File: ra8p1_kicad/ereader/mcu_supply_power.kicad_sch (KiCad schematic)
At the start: 20 parts, among them U1 R7KA8P1KFLCAC#UC0

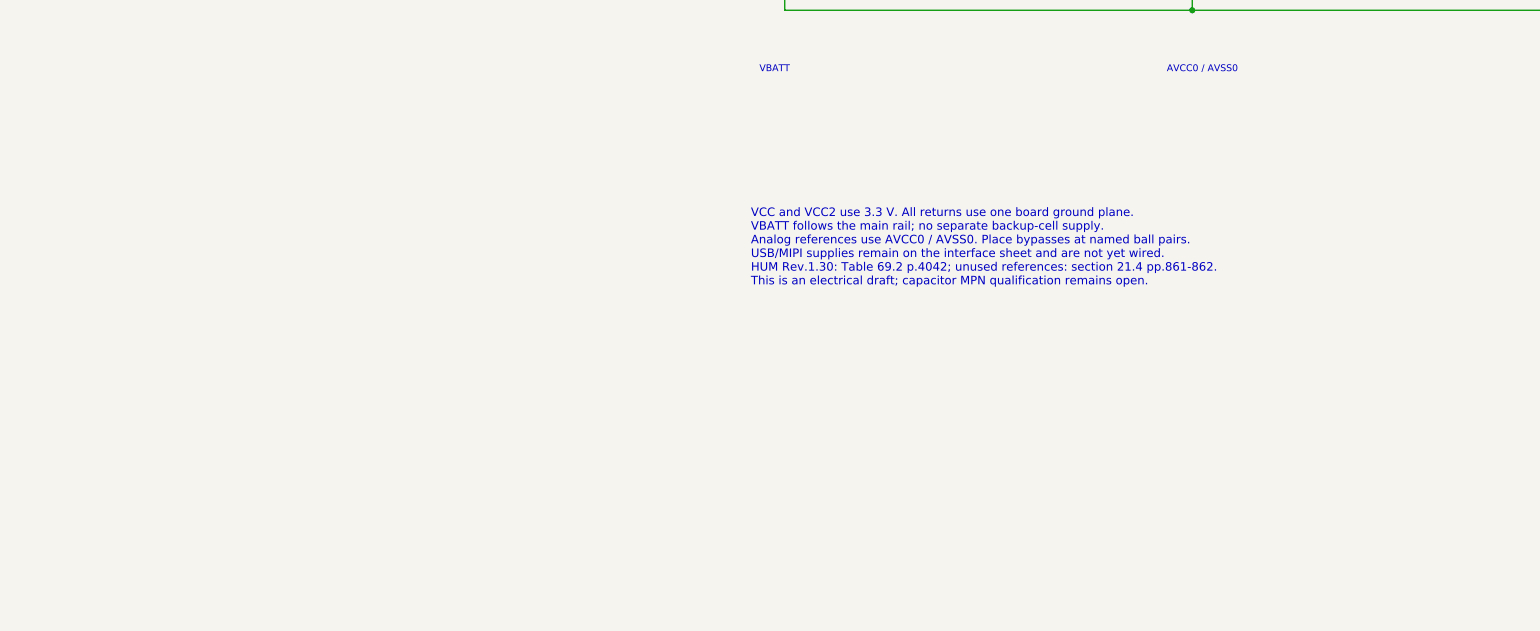
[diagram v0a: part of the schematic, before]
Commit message: hardware: integrate MIPI host 1.8V supply and bypass (#824, #841)
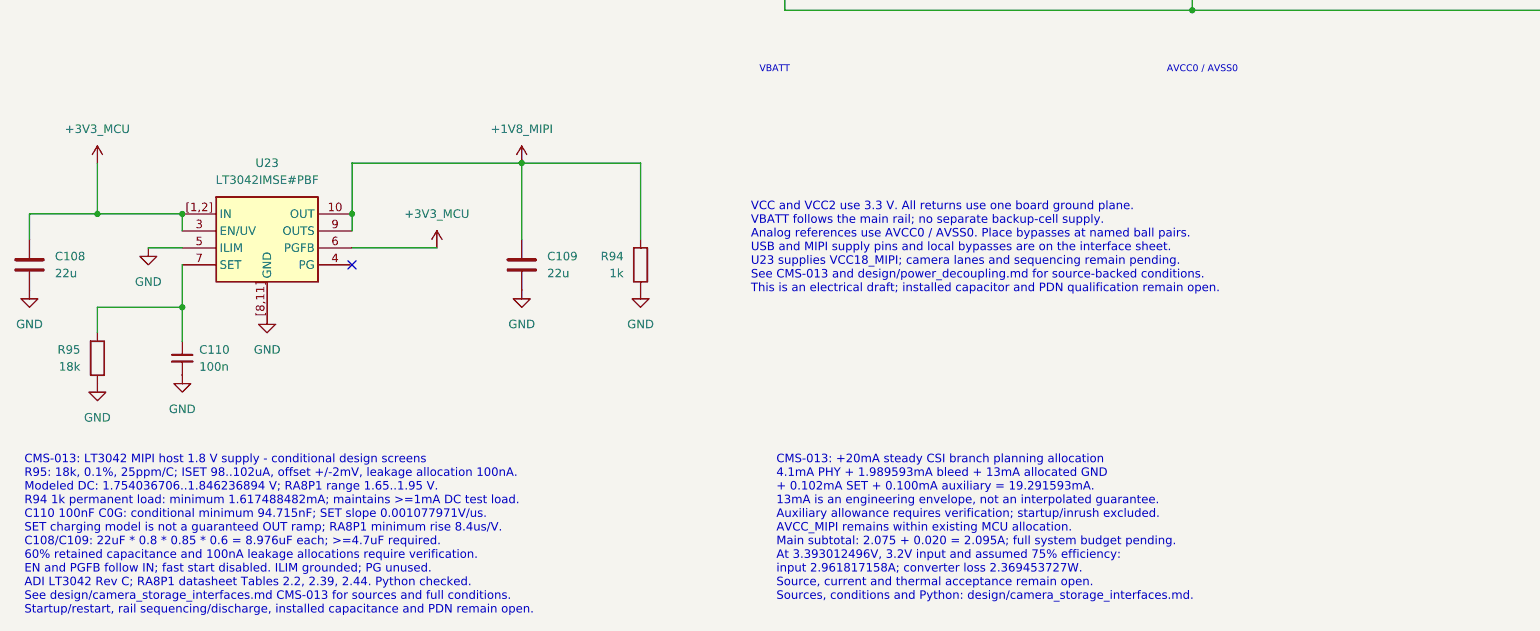
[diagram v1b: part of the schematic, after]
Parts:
- added C108, C109: 22u, symbol Device:C
- added C110: 100n, symbol Device:C_Small
- added R94: 1k, symbol Device:R
- added R95: 18k, symbol Device:R
- added U23: LT3042IMSE#PBF, Package_SO:MSOP-10-1EP_3x3mm_P0.5mm_EP1.68x1.88mm, symbol Power_Devices:LT3042IMSE#PBF
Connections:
- net +3V3_MCU: now also C108.1, U23.3 (EN/UV), U23.6 (PGFB), U23.[1,2] (IN)
- net GND: now also C108.2, C109.2, C110.2, R94.1, R95.1, U23.5 (ILIM), U23.[8,11] (GND)
- new net: C110.1, R95.2, U23.7 (SET)
- new net +1V8_MIPI: C109.1, R94.2, U23.10 (OUT), U23.9 (OUTS)
- no-connect marks 0 -> 1
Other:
- note added: "CMS-013: +20mA steady CSI branch planning allocation 4.1mA PHY + 1.989593mA bleed + 13mA allocated GND + 0.102mA SET + 0.100mA auxiliary = 19.291593mA. 13mA is an engineering envelope, not an interpolated guarantee. Auxiliary allowance requires verification; startup/inrush excluded. AVCC_MIPI remains within existing MCU allocation. Main subtotal: 2.075 + 0.020 = 2.095A; full system budget pending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"
- note added: "CMS-013: LT3042 MIPI host 1.8 V supply - conditional design screens R95: 18k, 0.1%, 25ppm/C; ISET 98..102uA, offset +/-2mV, leakage allocation 100nA. Modeled DC: 1.754036706..1.846236894 V; RA8P1 range 1.65..1.95 V. R94 1k permanent load: minimum 1.617488482mA; maintains >=1mA DC test load. C110 100nF C0G: conditional minimum 94.715nF; SET slope 0.001077971V/us. SET charging model is not a guaran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"
- note added: "VCC and VCC2 use 3.3 V. All returns use one board ground plane. VBATT follows the main rail; no separate backup-cell supply. Analog references use AVCC0 / AVSS0. Place bypasses at named ball pairs. USB and MIPI supply pins and local bypasses are on the interface sheet. U23 supplies VCC18_MIPI; camera lanes and sequencing remain pending. See CMS-013 and design/power_decoupling.md for source-backed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"
- note removed: "VCC and VCC2 use 3.3 V. All returns use one board ground plane. VBATT follows the main rail; no separate backup-cell supply. Analog references use AVCC0 / AVSS0. Place bypasses at named ball pairs. USB/MIPI supplies remain on the interface sheet and are not yet wired. HUM Rev.1.30: Table 69.2 p.4042; unused references: section 21.4 pp.861-862. This is an electrical draft; capacitor MPN qualificat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"

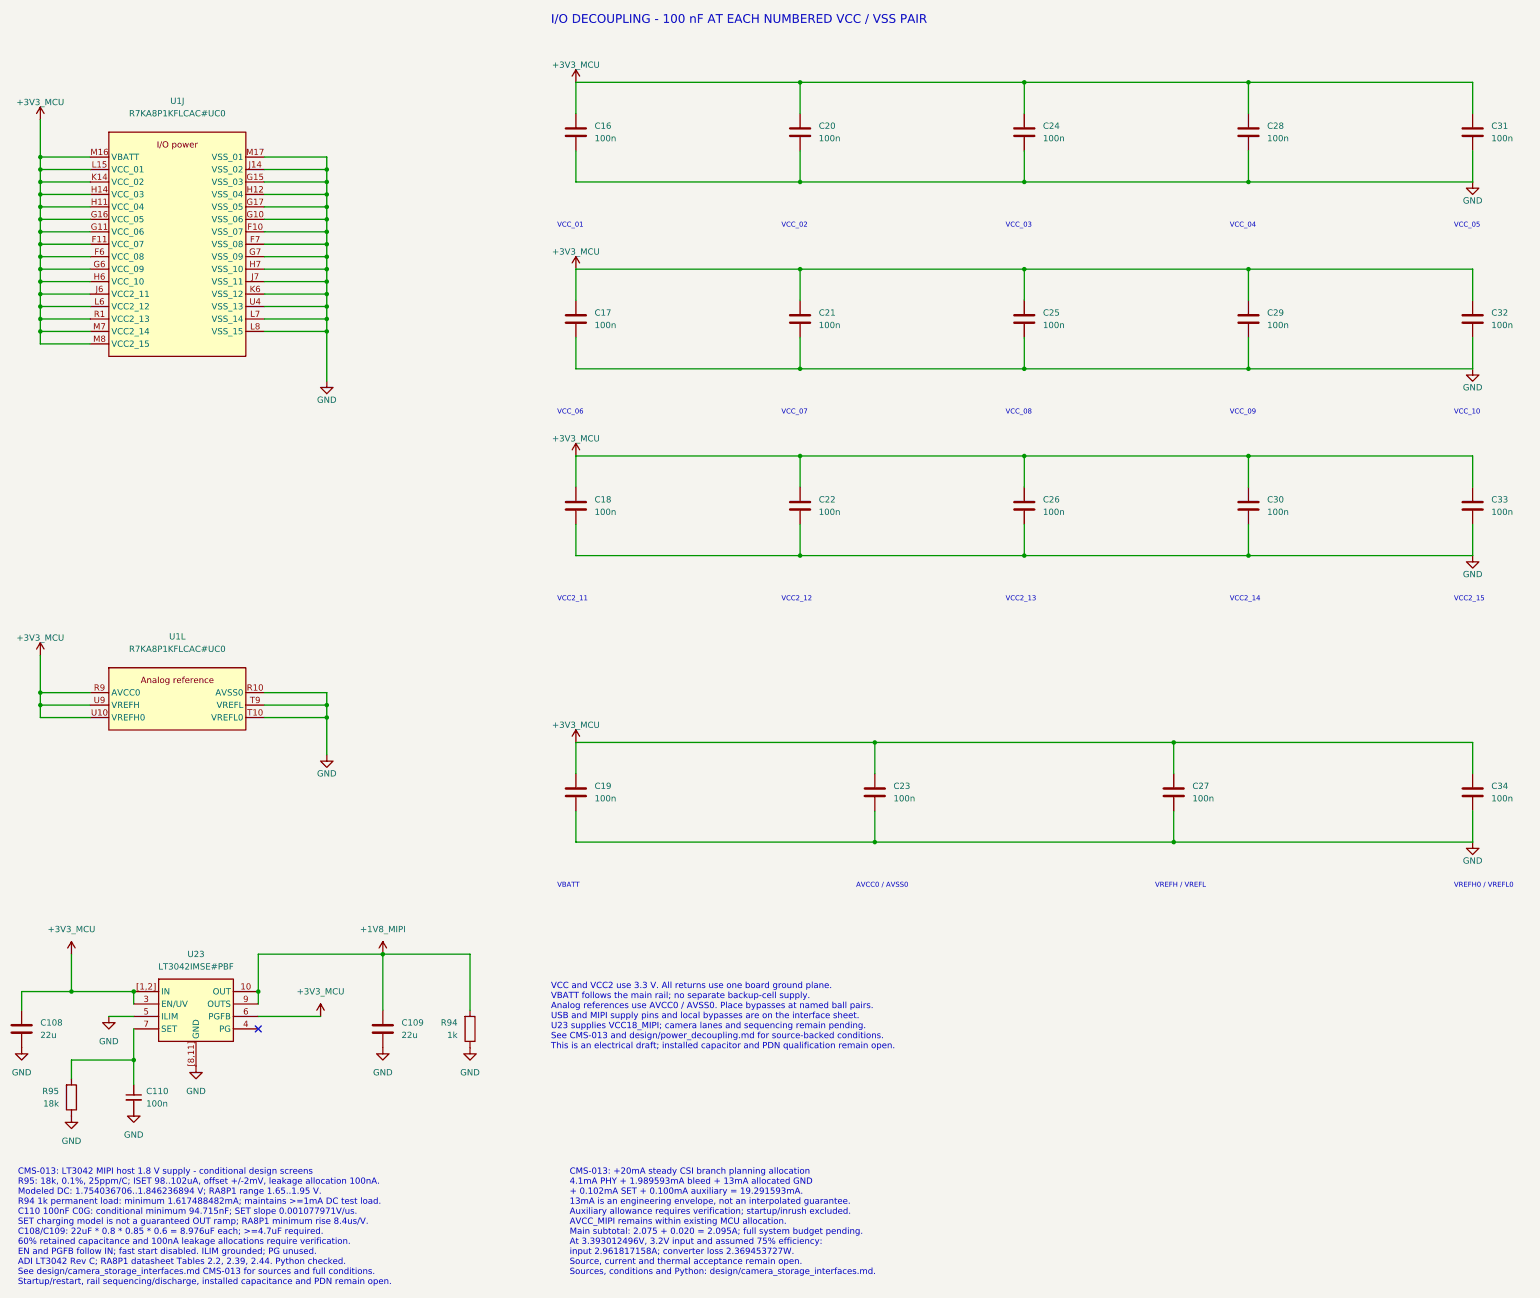
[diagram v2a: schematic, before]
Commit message: wip(hardware): preserve schematic cleanup and CEU host ports
Checkpoint cosmetic cleanup across the schematic hierarchy and eleven parallel-camera host ports. Refresh the complete 13-page PDF. All 334 existing net partitions and 271 component records match the prior CEU checkpoint; all 128 ERC identities remain unchanged. Electrical design is incomplete; this is a WIP checkpoint for #821 and #841.
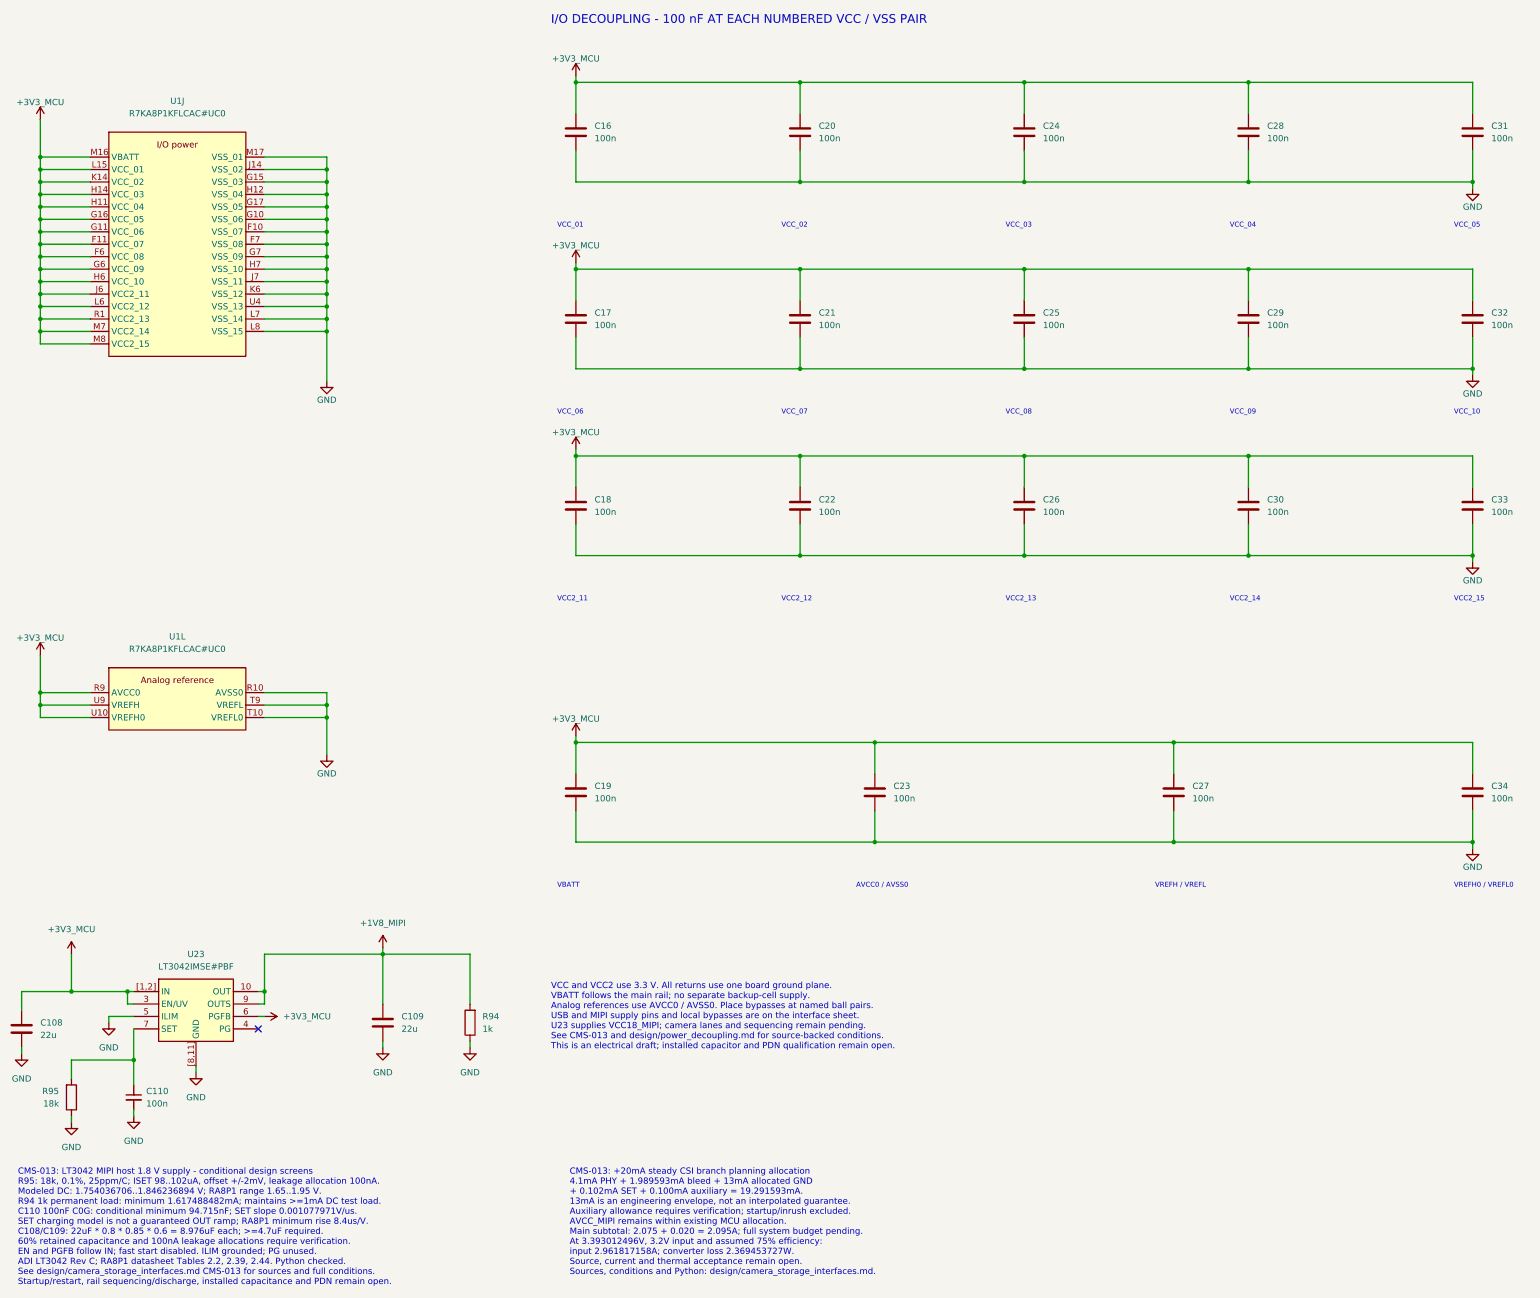
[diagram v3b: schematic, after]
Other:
- moved on the sheet: C109, R94
